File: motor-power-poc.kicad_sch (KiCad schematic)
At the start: 46 parts, among them SW1 SW_Push, SW2 SW_Push, U1 ESP32-S3FH4R2, U10 QRE1113GR, U8 QRE1113GR, U9 QRE1113GR, Y1 48M

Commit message: schem: add test points
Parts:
- added TP8: TestPoint, symbol Connector:TestPoint
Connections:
- net SO: now also TP8.1
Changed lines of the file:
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@@
 	)
 	(junction
+		(at 237.49 107.95)
+		(diameter 0)
+		(color 0 0 0 0)
+	)
+	(junction
 		(at 128.27 44.45)
 		(diameter 0)
@@
 	(wire
 		(pts
+			(xy 232.41 107.95) (xy 237.49 107.95)
+		)
+		(stroke
+			(width 0)
+			(type default)
+		)
+	)
+	(wire
+		(pts
 			(xy 142.24 54.61) (xy 142.24 55.88)
 		)
@@
 	(wire
 		(pts
-			(xy 232.41 107.95) (xy 236.22 107.95)
-		)
-		(stroke
-			(width 0)
-			(type default)
-		)
-	)
-	(wire
-		(pts
 			(xy 152.4 44.45) (xy 154.94 44.45)
 		)
@@
 	(wire
 		(pts
+			(xy 237.49 107.95) (xy 240.03 107.95)
+		)
+		(stroke
+			(width 0)
+			(type default)
+		)
+	)
+	(wire
+		(pts
 			(xy 248.92 67.31) (xy 250.19 67.31)
 		)
@@
 	(global_label "SO"
 		(shape input)
-		(at 236.22 107.95 0)
+		(at 240.03 107.95 0)
 		(effects
 			(font
@@
 		)
 		(property "Intersheetrefs" "${INTERSHEET_REFS}"
-			(at 236.22 107.95 0)
+			(at 240.03 107.95 0)
 			(effects
 				(font
@@
 					(unit 1)
 				)
+			)
+		)
+	)
+	(symbol
+		(lib_id "Connector:TestPoint")
+		(at 237.49 107.95 0)
+		(unit 1)
+		(exclude_from_sim no)
+		(in_bom yes)
+		(on_board yes)
+		(dnp no)
+		(property "Reference" "TP8"
+			(at 239.268 104.648 0)
+			(effects
+				(font
+					(size 1.27 1.27)
+				)
+				(justify left)
+			)
+		)
+		(property "Value" "TestPoint"
+			(at 240.03 105.9179 0)
+			(effects
+				(font
+					(size 1.27 1.27)
+				)
+				(justify left)
+				(hide yes)
+			)
+		)
+		(property "Footprint" ""
+			(at 242.57 107.95 0)
+			(effects
+				(font
+					(size 1.27 1.27)
+				)
+				(hide yes)
+			)
+		)
+		(property "Datasheet" "~"
+			(at 242.57 107.95 0)
+			(effects
+				(font
+					(size 1.27 1.27)
+				)
+				(hide yes)
+			)
+		)
+		(property "Description" "test point"
+			(at 237.49 107.95 0)
+			(effects
+				(font
+					(size 1.27 1.27)
+				)
+				(hide yes)
+			)
+		)
+		(pin "1"
+		)
+		(instances
+			(project "motor-power-poc"
+				(path "/a1dc4c9e-7b20-4b66-a693-9133bc644c6b"
+					(reference "TP8")
+					(unit 1)
+				)

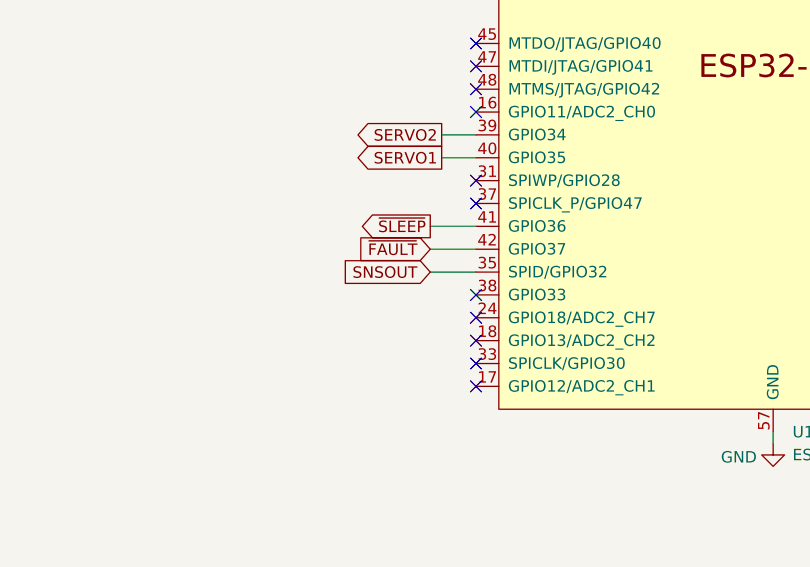
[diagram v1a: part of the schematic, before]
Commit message: schem: fix peripherals using flash ESP32 pins
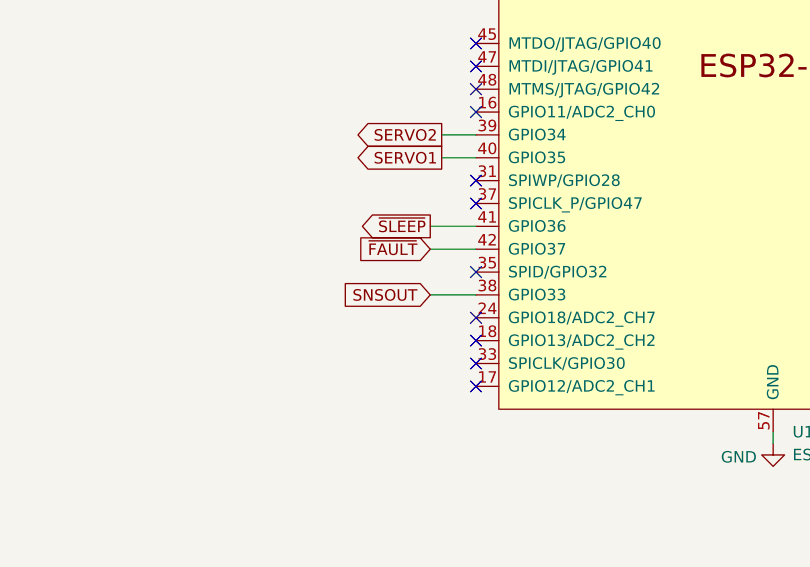
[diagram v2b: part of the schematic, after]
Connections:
- net SNSOUT: now also U1.38 (GPIO33); no longer U1.35 (SPID/GPIO32)
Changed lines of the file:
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@@
+	)
+	(no_connect
+		(at 166.37 115.57)
 	)
 	(no_connect
@@
 	)
 	(no_connect
-		(at 166.37 118.11)
-	)
-	(no_connect
 		(at 166.37 120.65)
 	)
@@
 	(wire
 		(pts
+			(xy 161.29 118.11) (xy 166.37 118.11)
+		)
+		(stroke
+			(width 0)
+			(type default)
+		)
+	)
+	(wire
+		(pts
 			(xy 182.88 46.99) (xy 182.88 48.26)
 		)
@@
 		(pts
 			(xy 46.99 26.67) (xy 52.07 26.67)
-		)
-		(stroke
-			(width 0)
-			(type default)
-		)
-	)
-	(wire
-		(pts
-			(xy 161.29 115.57) (xy 166.37 115.57)
 		)
 		(stroke
@@
 		)
 	)
+	(global_label "SNSOUT"
+		(shape input)
+		(at 161.29 118.11 180)
+		(effects
+			(font
+				(size 1.27 1.27)
+			)
+			(justify right)
+		)
+		(property "Intersheetrefs" "${INTERSHEET_REFS}"
+			(at 161.29 118.11 0)
+			(effects
+				(font
+					(size 1.27 1.27)
+				)
+				(hide yes)
+			)
+		)
+	)
 	(global_label "PH"
 		(shape output)
@@
 			(effects
 				(font
-					(size 1.27 1.27)
-				)
-				(hide yes)
-			)
-		)
-	)
-	(global_label "SNSOUT"
-		(shape input)
-		(at 161.29 115.57 180)
-		(effects
-			(font
-				(size 1.27 1.27)
-			)
-			(justify right)
-		)
-		(property "Intersheetrefs" "${INTERSHEET_REFS}"
-			(at 161.29 115.57 0)
-			(effects
-				(font

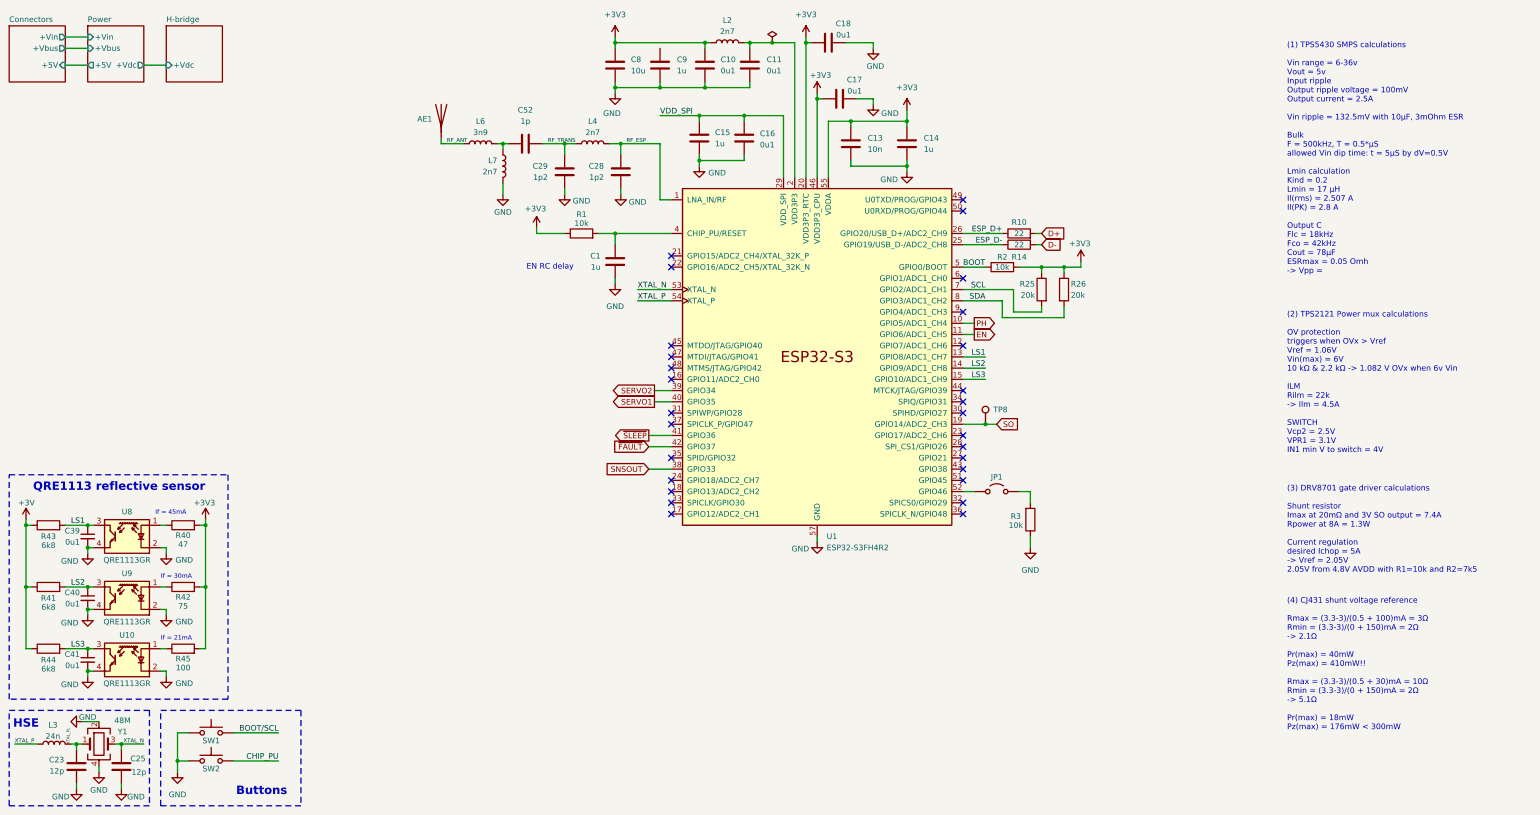
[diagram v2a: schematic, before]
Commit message: schem: renumber
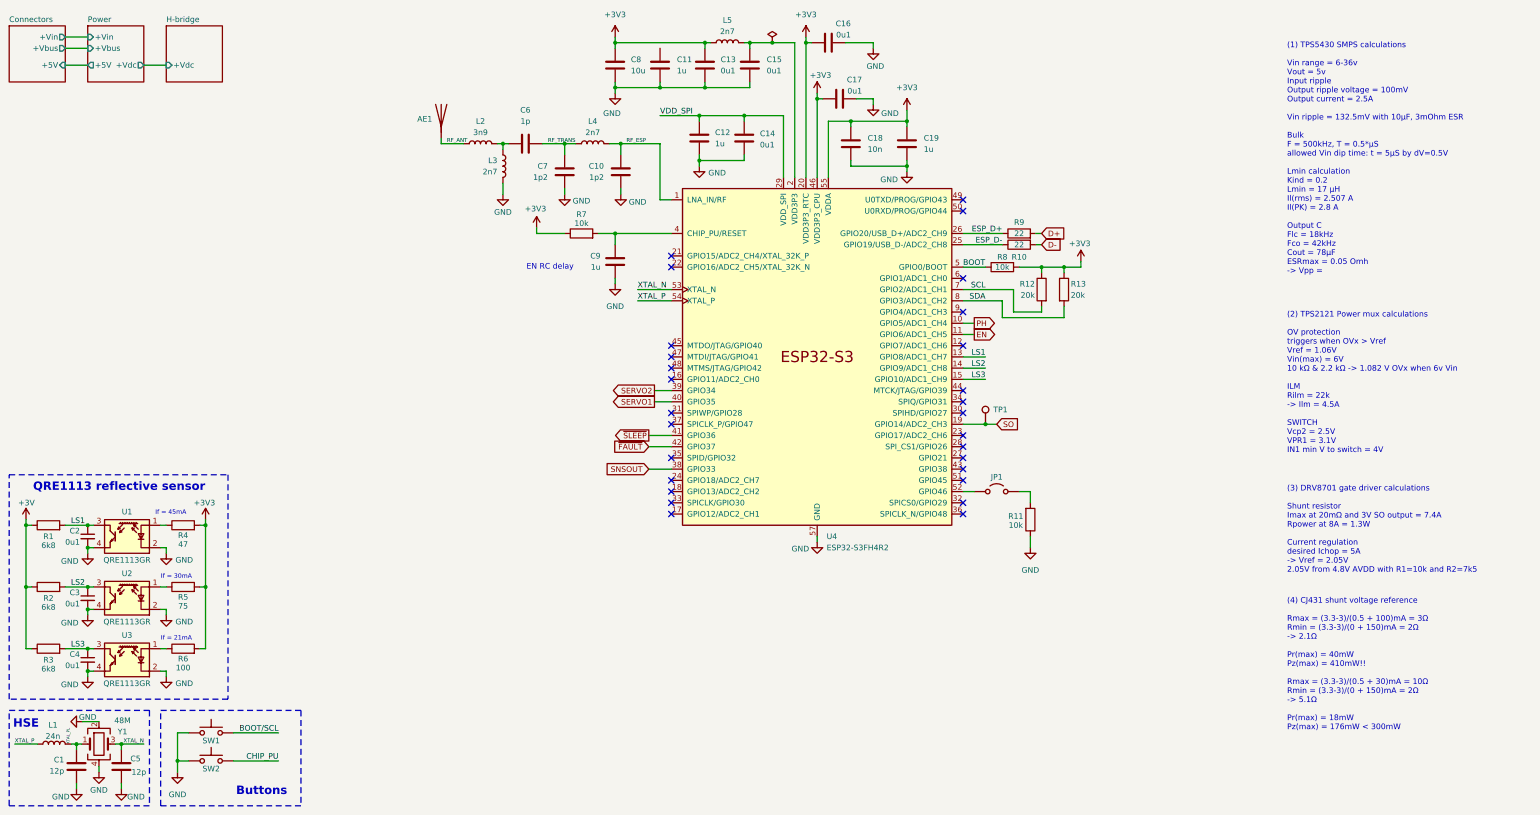
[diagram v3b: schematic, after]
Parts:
- renumbered C23 to C1, C28 to C10, C9 to C11, C15 to C12, C10 to C13, C16 to C14, C11 to C15, C18 to C16, C13 to C18, C14 to C19, C39 to C2, C40 to C3, C41 to C4, C25 to C5, C52 to C6, C29 to C7, C1 to C9, L3 to L1, L6 to L2, L7 to L3, L2 to L5, R43 to R1, R14 to R10, R3 to R11, R25 to R12, R26 to R13, R41 to R2, R44 to R3, R40 to R4, R42 to R5, R45 to R6, R1 to R7, R2 to R8, R10 to R9, TP8 to TP1, U8 to U1, U9 to U2, U10 to U3, U1 to U4

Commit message: schem: run and fix ERC
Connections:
- net BOOT/SCL is gone; now on net BOOT: SW1.2
- net +3V3: now also C11.1
- net CHIP_PU: now also C9.1, R7.2, U4.4 (CHIP_PU/RESET)
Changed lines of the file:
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@@
+	)
+	(junction
+		(at 163.83 21.59)
+		(diameter 0)
+		(color 0 0 0 0)
 	)
 	(junction
@@
 	(wire
 		(pts
-			(xy 153.67 21.59) (xy 173.99 21.59)
+			(xy 153.67 21.59) (xy 163.83 21.59)
 		)
 		(stroke
@@
 	(wire
 		(pts
+			(xy 163.83 21.59) (xy 163.83 22.86)
+		)
+		(stroke
+			(width 0)
+			(type default)
+		)
+	)
+	(wire
+		(pts
 			(xy 17.78 180.34) (xy 22.86 180.34)
 		)
@@
 	(wire
 		(pts
+			(xy 163.83 21.59) (xy 173.99 21.59)
+		)
+		(stroke
+			(width 0)
+			(type default)
+		)
+	)
+	(wire
+		(pts
 			(xy 219.71 49.53) (xy 207.01 49.53)
 		)
@@
 		)
 	)
-	(label "BOOT{slash}SCL"
+	(label "CHIP_PU"
+		(at 163.83 64.77 180)
+		(effects
+			(font
+				(size 1.27 1.27)
+			)
+			(justify right bottom)
+		)
+	)
+	(label "BOOT"
 		(at 77.47 177.8 180)
 		(effects

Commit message: schem: add net classes
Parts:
- removed R12, R13: 20k, Resistor_SMD:R_0402_1005Metric, symbol Device:R
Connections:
- net SCL: no longer names the net of U4.7 (GPIO2/ADC1_CH1)
- net SDA: no longer names the net of U4.8 (GPIO3/ADC1_CH2)
- no-connect marks 28 -> 30

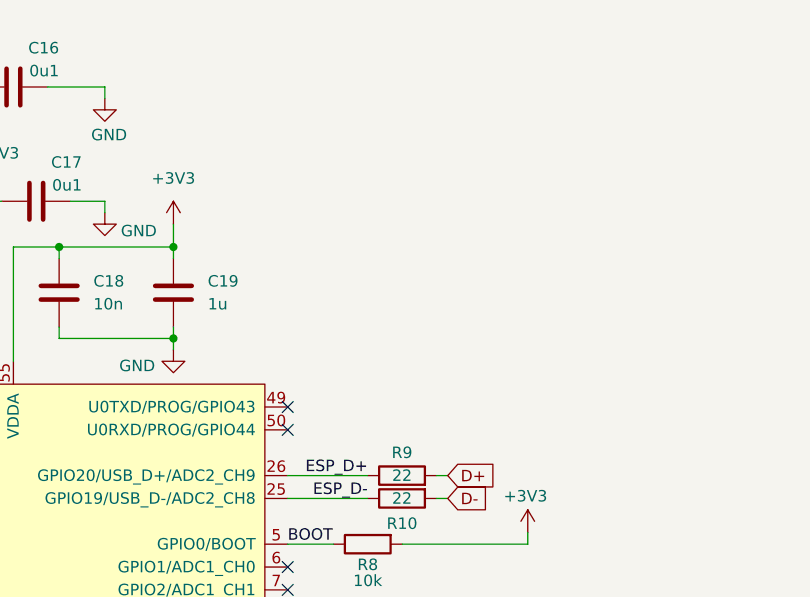
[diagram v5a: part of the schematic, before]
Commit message: schem: import UART connector from esp32c6-sensor-devboard
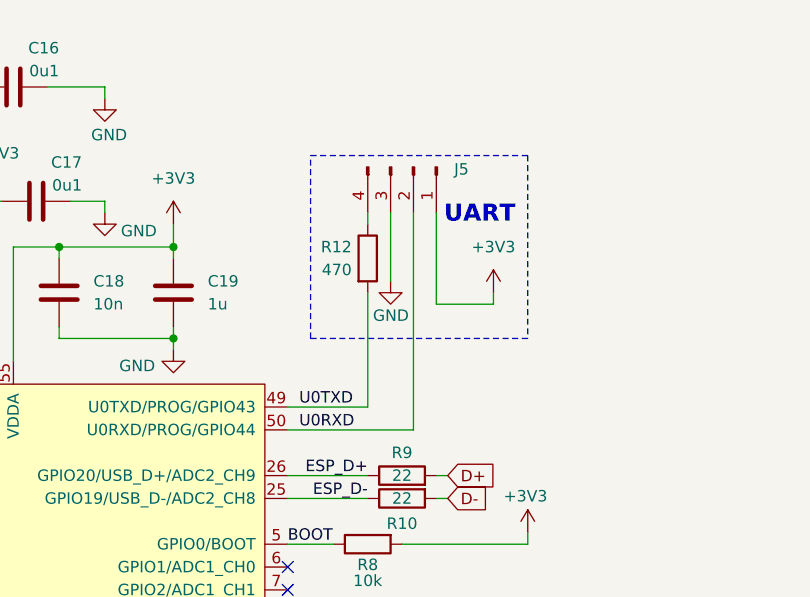
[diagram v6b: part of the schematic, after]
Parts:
- added J5: Conn_01x04_Pin, Connector_PinHeader_2.54mm:PinHeader_1x04_P2.54mm_Vertical, symbol Connector:Conn_01x04_Pin
- added R12: 470, Resistor_SMD:R_0402_1005Metric, symbol Device:R
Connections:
- net +3V3: now also J5.1 (Pin_1)
- net GND: now also J5.3 (Pin_3)
- net U0TXD: now reaches U4.49 (U0TXD/PROG/GPIO43)
- net U0TXD: now also R12.2
- net U0RXD: now reaches U4.50 (U0RXD/PROG/GPIO44)
- net U0RXD: now also J5.2 (Pin_2)
- new net: J5.4 (Pin_4), R12.1
- no-connect marks 30 -> 28
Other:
- note added: "UART"

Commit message: schem: add title
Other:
- company: (none) -> Rémi Ait-Younes
- title: (none) -> Motor Power POC
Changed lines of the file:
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@@
 	(generator_version "9.0")
 	(paper "A4")
+	(title_block
+		(title "Motor Power POC")
+		(date "2025-11-30")
+		(rev "01")
+		(company "Rémi Ait-Younes")
+	)
 	(rectangle
 		(start 50.8 172.72)

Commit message: schem: assign footprints
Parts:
- C2, C3, C4: footprint (none) -> Capacitor_SMD:C_0402_1005Metric
- R1, R2, R3: footprint (none) -> Resistor_SMD:R_0402_1005Metric
- R4, R5, R6: footprint (none) -> Resistor_SMD:R_0603_1608Metric
- TP1: footprint (none) -> GLCS:TestPoint_Keystone_5015_Micro_Mini
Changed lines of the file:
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@@
 			)
 		)
-		(property "Footprint" ""
+		(property "Footprint" "Capacitor_SMD:C_0402_1005Metric"
 			(at 34.29 147.32 0)
 			(effects
@@
 			)
 		)
-		(property "Footprint" ""
+		(property "Footprint" "Capacitor_SMD:C_0402_1005Metric"
 			(at 34.29 161.29 0)
 			(effects
@@
 			)
 		)
-		(property "Footprint" ""
+		(property "Footprint" "Resistor_SMD:R_0603_1608Metric"
 			(at 55.88 146.558 90)
 			(effects
@@
 			)
 		)
-		(property "Footprint" ""
+		(property "Footprint" "Resistor_SMD:R_0402_1005Metric"
 			(at 25.4 160.528 90)
 			(effects
@@
 			)
 		)
-		(property "Footprint" ""
+		(property "Footprint" "Resistor_SMD:R_0402_1005Metric"
 			(at 25.4 146.558 90)
 			(effects
@@
 			)
 		)
-		(property "Footprint" ""
+		(property "Footprint" "GLCS:TestPoint_Keystone_5015_Micro_Mini"
 			(at 242.57 107.95 0)
 			(effects
@@
 			)
 		)
-		(property "Footprint" ""
+		(property "Footprint" "Resistor_SMD:R_0603_1608Metric"
 			(at 55.88 132.588 90)
 			(effects
@@
 			)
 		)
-		(property "Footprint" ""
+		(property "Footprint" "Resistor_SMD:R_0603_1608Metric"
 			(at 55.88 160.528 90)
 			(effects
@@
 			)
 		)
-		(property "Footprint" ""
+		(property "Footprint" "Capacitor_SMD:C_0402_1005Metric"
 			(at 34.29 133.35 0)
 			(effects
@@
 			)
 		)
-		(property "Footprint" ""
+		(property "Footprint" "Resistor_SMD:R_0402_1005Metric"
 			(at 25.4 132.588 90)
 			(effects
